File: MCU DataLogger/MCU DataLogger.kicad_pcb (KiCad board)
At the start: 2 copper layers, 50 x 30 mm, 29 parts, among them J1 Conn_01x04_Pin, J2 Conn_01x04_Pin, J3 Conn_01x09_Pin, J4 Conn_02x03_Odd_Even, U1 24LC1025, U2 DS1337S_, U3 ATMEGA328P-AN, U4 24LC1025, Y1 32.768 KHz, Y2 16MHz

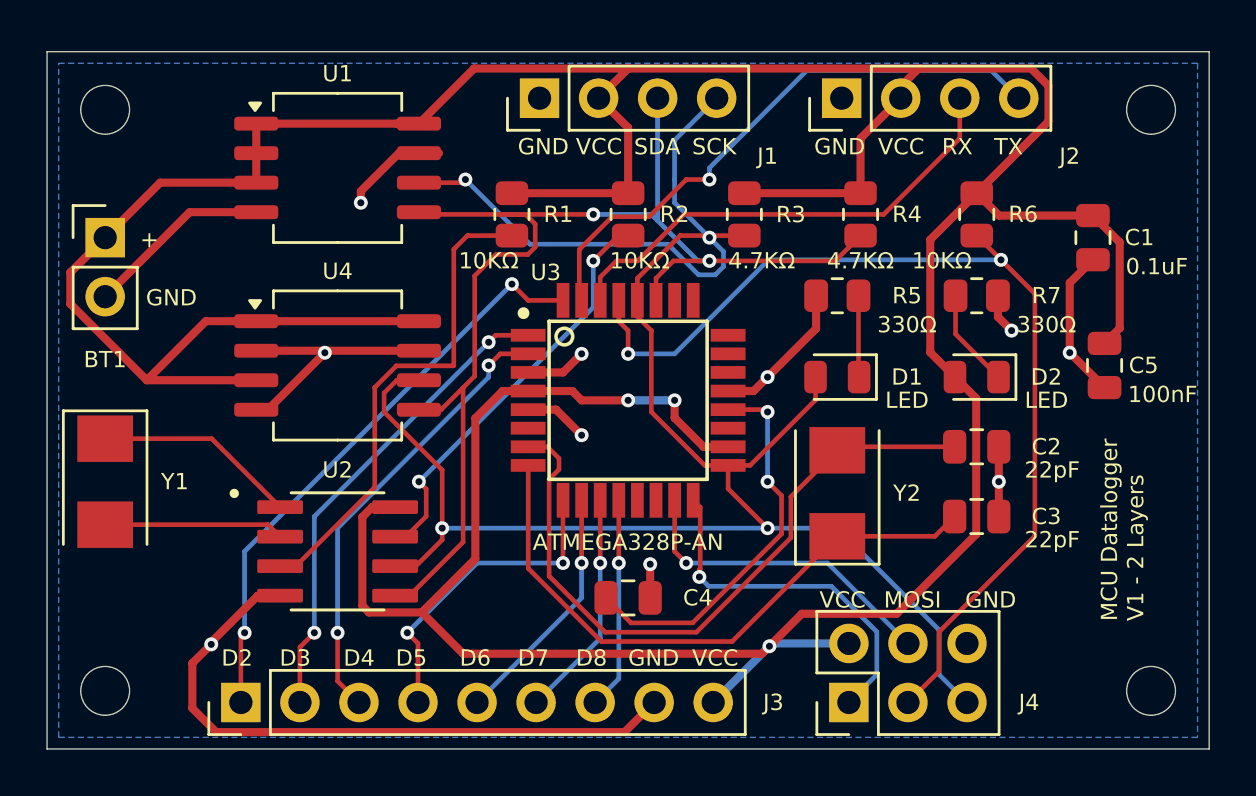
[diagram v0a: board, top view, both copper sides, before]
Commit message: MCU DataLogger Enhance 2Layers Version
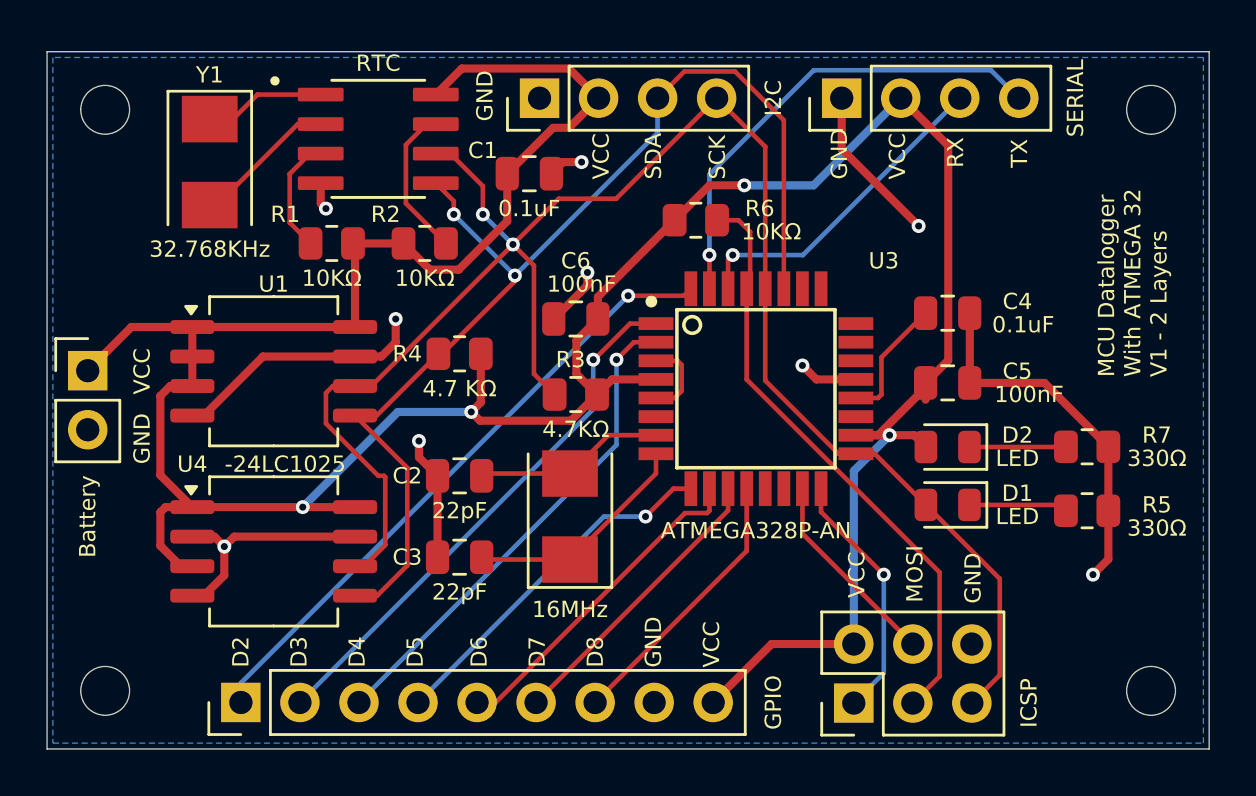
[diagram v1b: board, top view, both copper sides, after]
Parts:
- removed BT1: Battery, Connector_PinHeader_2.54mm:PinHeader_1x02_P2.54mm_Vertical
- added Battery: Battery, Connector_PinHeader_2.54mm:PinHeader_1x02_P2.54mm_Vertical, F.Cu at (176.8, 98.7)
- added C6: 100nF, Capacitor_SMD:C_0805_2012Metric, F.Cu at (197.8, 96.5)
- R4: value 4.7KΩ -> 4.7 KΩ
- U1, U4: value 24LC1025 -> -24LC1025
- Y1: value 32.768 KHz -> 32.768KHz
- moved C1 24.4 mm to (195.8, 90.2), turned to 0 degrees
- moved C3 22.3 mm to (192.8, 106.8), turned to 0 degrees
- moved C2 22.3 mm to (192.8, 103.2), turned to 0 degrees
- moved C4 18.4 mm to (213.8, 96.2)
- moved R4 18.3 mm to (192.8, 98.0), turned to 180 degrees
- moved RTC 17.8 mm to (189.2, 88.8)
- moved Y1 14.5 mm to (182.0, 89.8)
- moved R5 14.2 mm to (219.8, 104.8), turned to 180 degrees
- moved R6 12.1 mm to (202.9, 92.2), turned to 180 degrees
- moved Y2 11.5 mm to (197.5, 105.0)
- moved R3 10.6 mm to (197.8, 99.8), turned to 180 degrees
- moved U1 9.17 mm to (184.8, 98.8)
- moved R2 8.84 mm to (191.2, 93.2), turned to 0 degrees
- moved U4 8.46 mm to (184.8, 106.5)
- moved R7 8.05 mm to (219.8, 102.0)
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- renumbered J3 to GPIO, J1 to I2C, J4 to ICSP, U2 to RTC, J2 to SERIAL
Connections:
- U3 pad 3: GND -> Net-(U3-GND-Pad3)
- U3 pad 5: GND -> Net-(U3-GND-Pad3)
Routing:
- net /VCC: track 193.3 -> 140.5 mm, vias 3 -> 4
- net Net-(U3-PB6): track 29.6 -> 8.22 mm
- net GND: track 75.8 -> 57.3 mm, vias 10 -> 9
- net /RESET: track 43.6 -> 25.9 mm, vias 2 -> 0
- net Net-(U3-PB7): track 27.0 -> 9.92 mm
- net Net-(U2-~{INTA}): track 21.3 -> 5.06 mm
- net Net-(U3-AREF): track 16.8 -> 5.45 mm, vias 2 -> 0
- net /SCK: track 87.8 -> 76.8 mm, vias 4 -> 2
- net Net-(U2-SQW/~INT): track 17.9 -> 7.25 mm, vias 2 -> 0
- net /RX: track 20.7 -> 14.1 mm, vias 0 -> 1
- net /MOSI: track 13.9 -> 8.65 mm, vias 1 -> 0
- net /MISO: track 15.6 -> 10.9 mm
- net /TX: track 25.1 -> 20.6 mm
- net Net-(U2-X1): track 8.74 -> 4.21 mm
- net /SDA: track 53.3 -> 49.3 mm
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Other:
- board text added: "MCU Datalogger With ATMEGA 32 V1 - 2 Layers"
- board text removed: "+"
- board text removed: "MCU Datalogger V1 - 2 Layers"
